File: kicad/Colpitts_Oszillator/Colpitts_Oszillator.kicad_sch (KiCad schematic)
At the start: 14 parts, among them Q1 2N3904

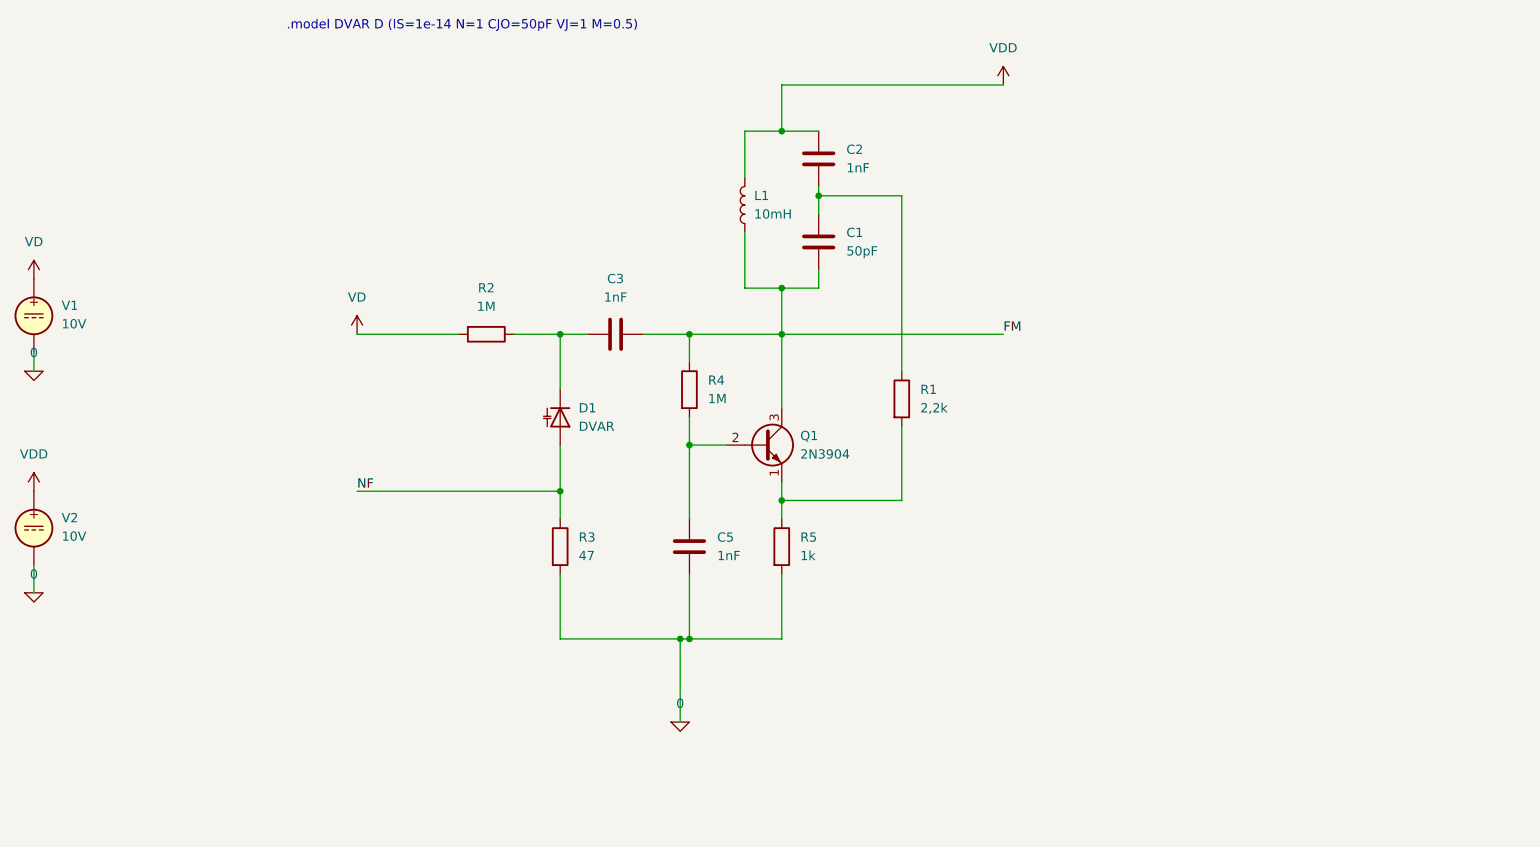
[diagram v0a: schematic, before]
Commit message: Colpitts-Oszillator_5_5MHz
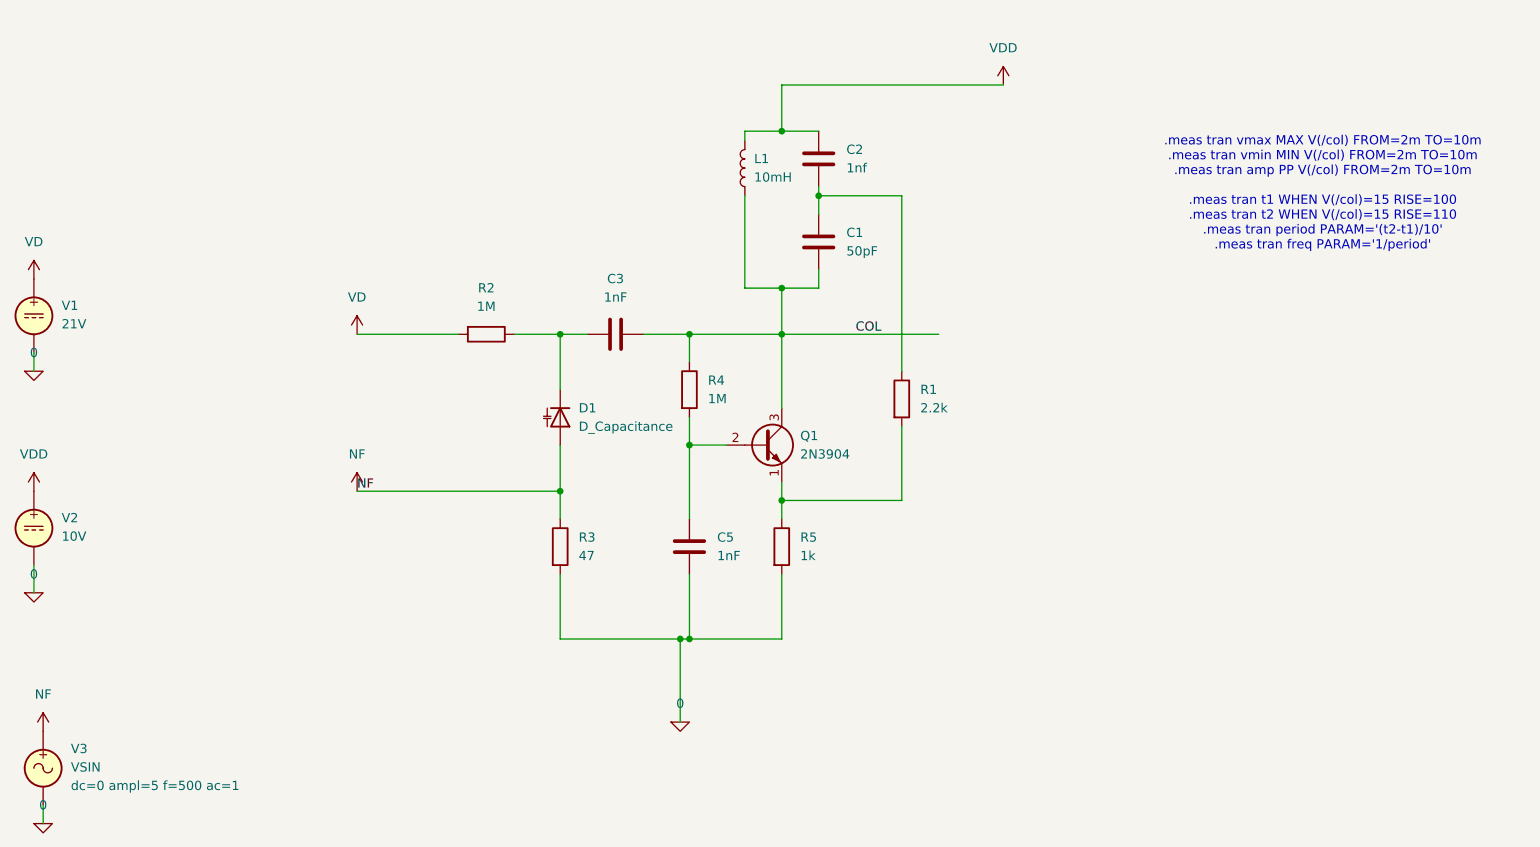
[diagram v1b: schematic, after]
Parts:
- added V3: VSIN, symbol Simulation_SPICE:VSIN
- C2: value 1nF -> 1nf
- D1: value DVAR -> D_Capacitance
- R1: value 2,2k -> 2.2k
- V1: value 10V -> 21V
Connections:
- net 0: now also V3.2
- net NF: now also V3.1
- net FM renamed COL
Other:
- note added: ".meas tran vmax MAX V(/col) FROM=2m TO=10m .meas tran vmin MIN V(/col) FROM=2m TO=10m .meas tran amp PP V(/col) FROM=2m TO=10m .meas tran t1 WHEN V(/col)=15 RISE=100 .meas tran t2 WHEN V(/col)=15 RISE=110 .meas tran period PARAM='(t2-t1)/10' .meas tran freq PARAM='1/period'"
- note removed: ".model DVAR D (IS=1e-14 N=1 CJO=50pF VJ=1 M=0.5)"
- moved on the sheet: L1
